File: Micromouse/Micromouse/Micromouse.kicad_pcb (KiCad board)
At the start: 4 copper layers, 75 x 101.5 mm, 51 parts, among them J1 motor1, J2 motor2, J3 Conn_01x06_Pin, J4 B2B-PH-K-S, J6 B2B-PH-K-S, J7 Conn_ARM_JTAG_SWD_10, Q1 2N7002K, U4 DRV8833RTY, U5 ISM330IS, U6 STM32G484RETx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

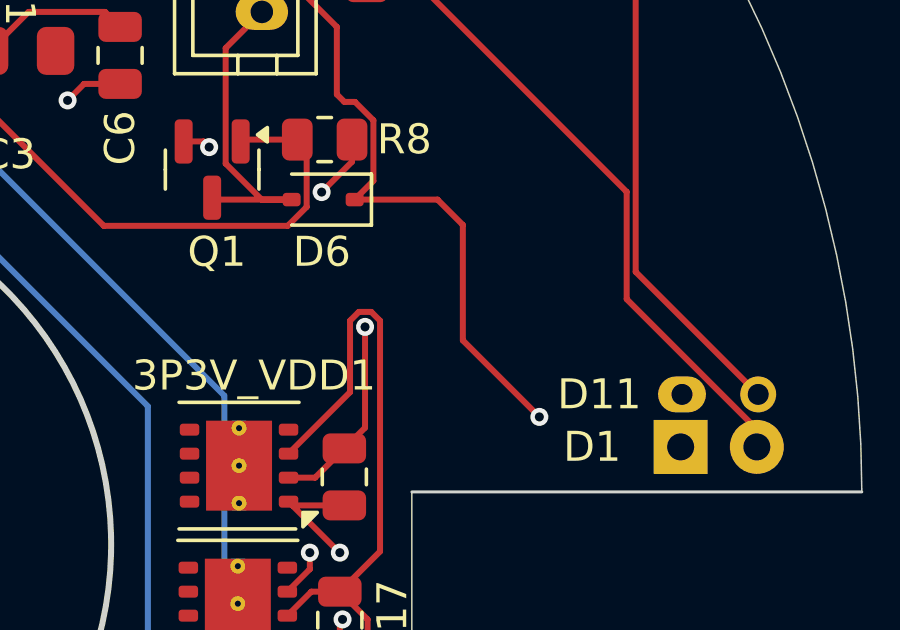
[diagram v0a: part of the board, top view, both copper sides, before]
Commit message: vdrive trace routing
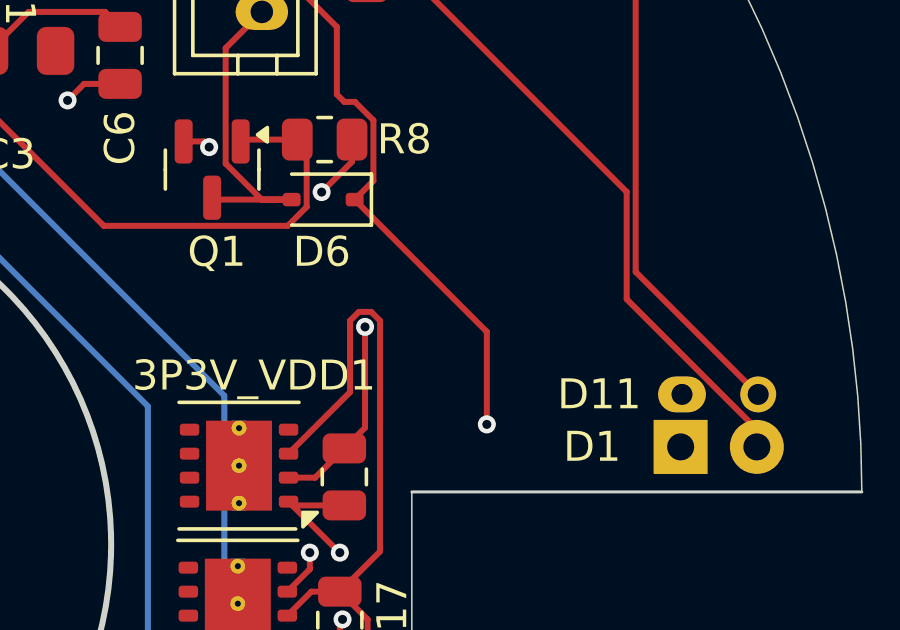
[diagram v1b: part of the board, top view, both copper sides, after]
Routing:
- net Vdrive: track 33.7 -> 31.6 mm
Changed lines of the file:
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@@
+	)
+	(segment
+		(start 175.34375 68.00625)
+		(end 179.75 72.4125)
+		(width 0.2)
+		(layer "F.Cu")
+		(net 78)
 	)
 	(segment
@@
 		(start 138.44375 82.39375)
 		(end 139.2125 83.1625)
-		(width 0.2)
-		(layer "F.Cu")
-		(net 78)
-	)
-	(segment
-		(start 178.95 68.85)
-		(end 178.10625 68.00625)
 		(width 0.2)
 		(layer "F.Cu")
@@
 	)
 	(segment
-		(start 178.95 72.7)
-		(end 178.95 68.85)
+		(start 179.75 72.4125)
+		(end 179.75 75.5)
 		(width 0.2)
 		(layer "F.Cu")
@@
 		(net 78)
 	)
-	(segment
-		(start 178.10625 68.00625)
-		(end 175.34375 68.00625)
-		(width 0.2)
-		(layer "F.Cu")
-		(net 78)
-	)
-	(segment
-		(start 181.5 75.25)
-		(end 178.95 72.7)
-		(width 0.2)
-		(layer "F.Cu")
-		(net 78)
-	)
 	(via
 		(at 173.85 79.775)
@@
 	)
 	(via
-		(at 181.5 75.25)
+		(at 179.75 75.5)
 		(size 0.6)
 		(drill 0.3)

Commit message: silkscreen
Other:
- board text added: "{dblquote}Mark 1{dblquote}"
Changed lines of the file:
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@@
 		(layer "Edge.Cuts")
+	)
+	(gr_text "{dblquote}Mark 1{dblquote}"
+		(at 170.25 141.25 0)
+		(layer "F.SilkS")
+		(effects
+			(font
+				(size 1 1)
+				(thickness 0.1)
+			)
+			(justify left bottom)
+		)
 	)
 	(segment
